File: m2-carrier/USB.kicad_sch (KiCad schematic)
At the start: 3 parts, among them P7 USB_C_Plug, U4 USBLC6-2SC6

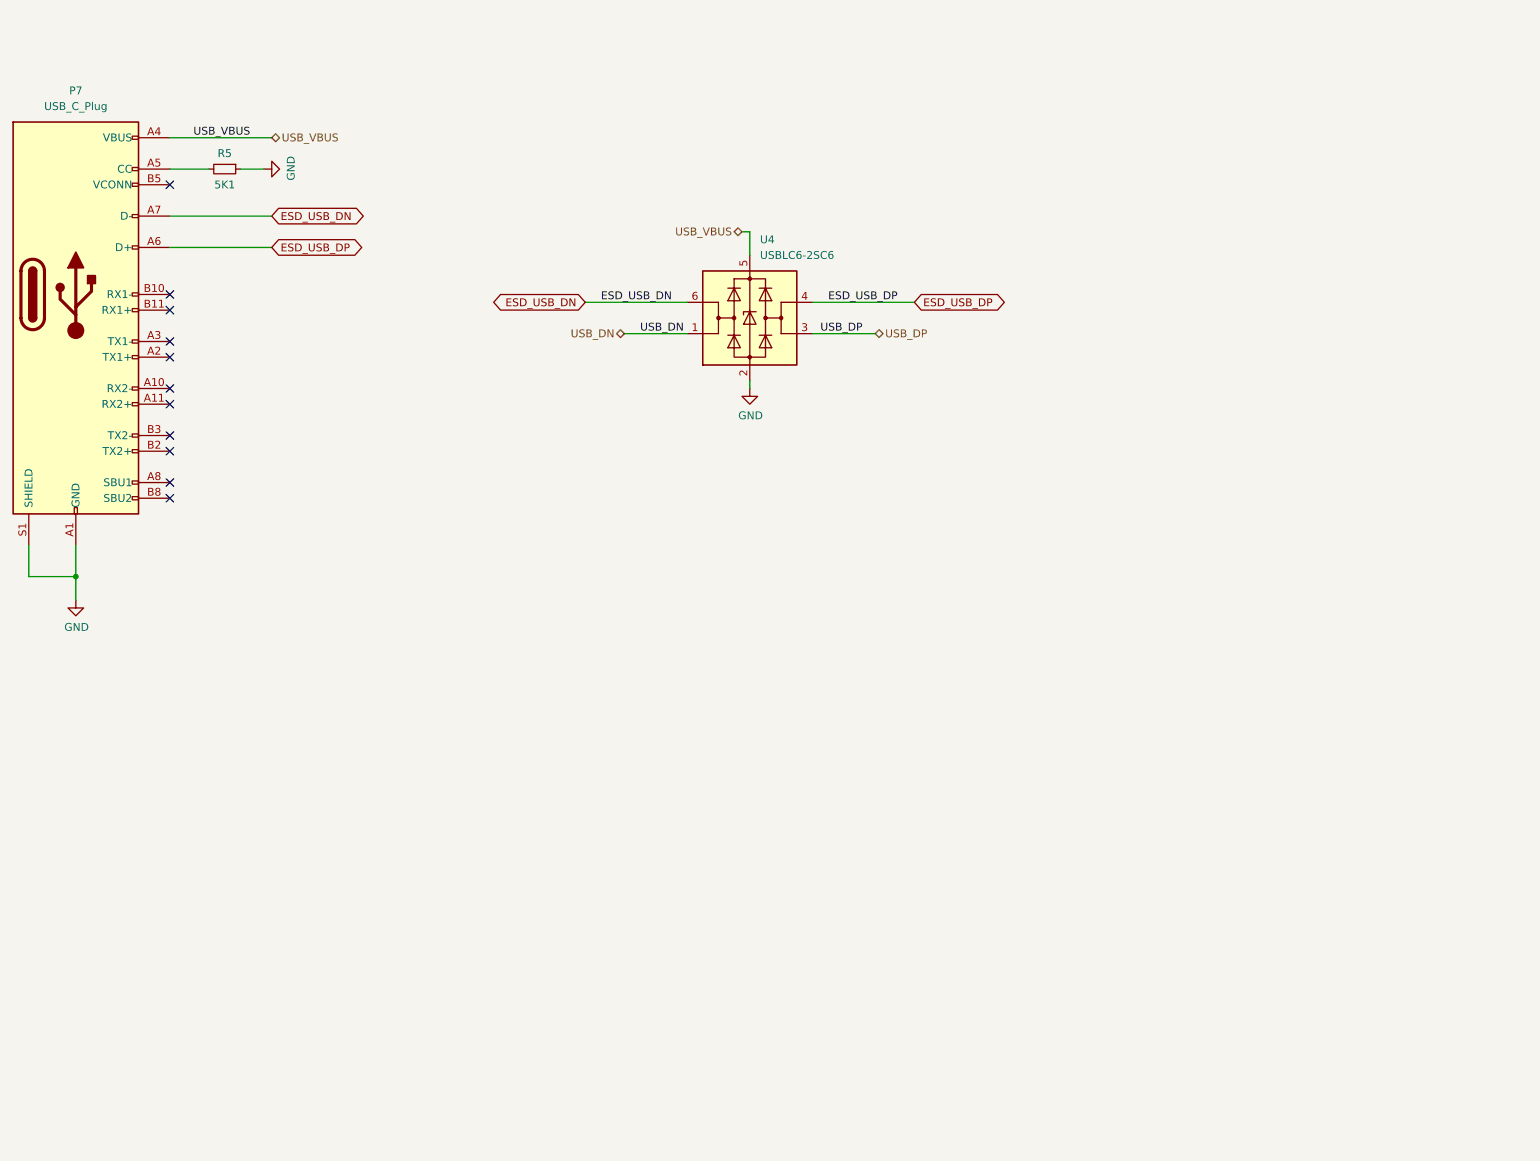
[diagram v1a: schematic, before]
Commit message: added video IC
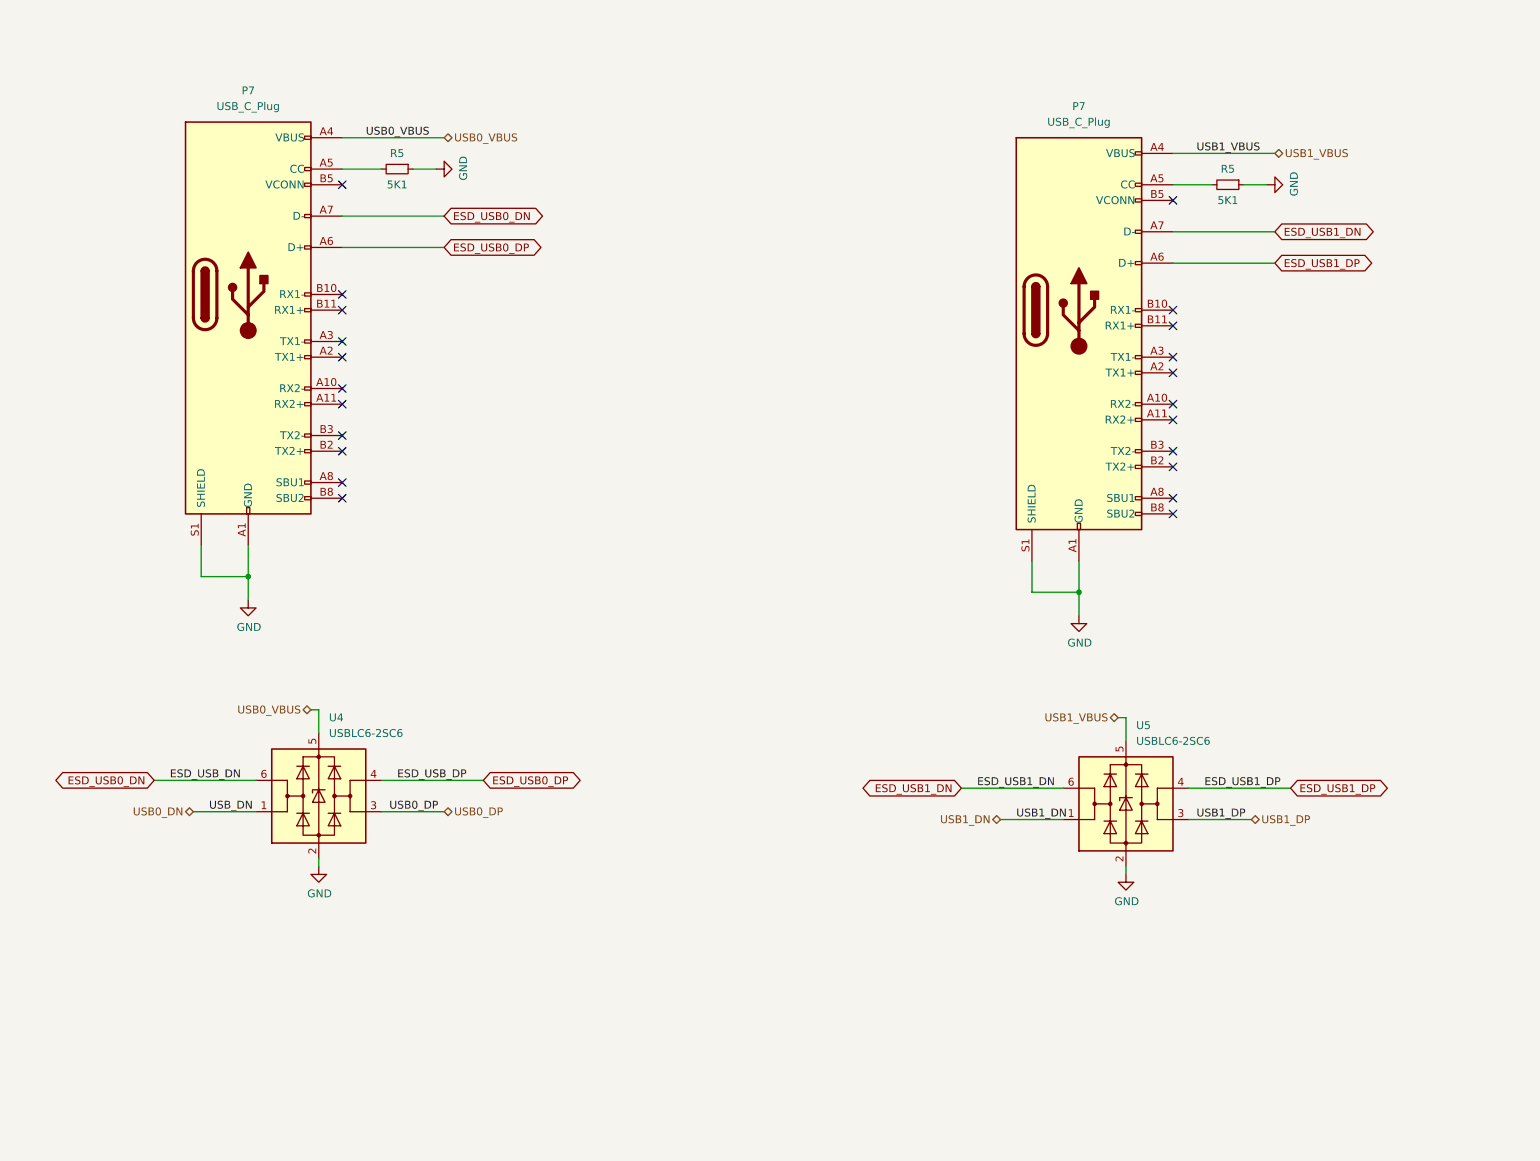
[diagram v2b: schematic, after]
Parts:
- added P7: USB_C_Plug, symbol Connector:USB_C_Plug
- added R5: 5K1, symbol Device:R_Small
- added U5: USBLC6-2SC6, Package_TO_SOT_SMD:SOT-23-6, symbol Power_Protection:USBLC6-2SC6
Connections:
- net GND: now also P7.A1 (GND), P7.A12 (GND), P7.B1 (GND), P7.B12 (GND), P7.S1 (SHIELD), R5.1, U5.2 (GND)
- net ESD_USB_DN renamed ESD_USB0_DN
- net ESD_USB_DP renamed ESD_USB0_DP
- net USB_DN renamed USB0_DN
- net USB_DP renamed USB0_DP
- net USB_VBUS renamed USB0_VBUS
- new net: P7.A5 (CC), R5.2
- new net ESD_USB1_DN: P7.A7 (D-), U5.6 (I/O1)
- new net ESD_USB1_DP: P7.A6 (D+), U5.4 (I/O2)
- new net USB1_DN: U5.1 (I/O1)
- new net USB1_DP: U5.3 (I/O2)
- new net USB1_VBUS: P7.A4 (VBUS), P7.A9 (VBUS), P7.B4 (VBUS), P7.B9 (VBUS), U5.5 (VBUS)
- no-connect marks 11 -> 22
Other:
- moved on the sheet: P7, R5, U4

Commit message: Added base board
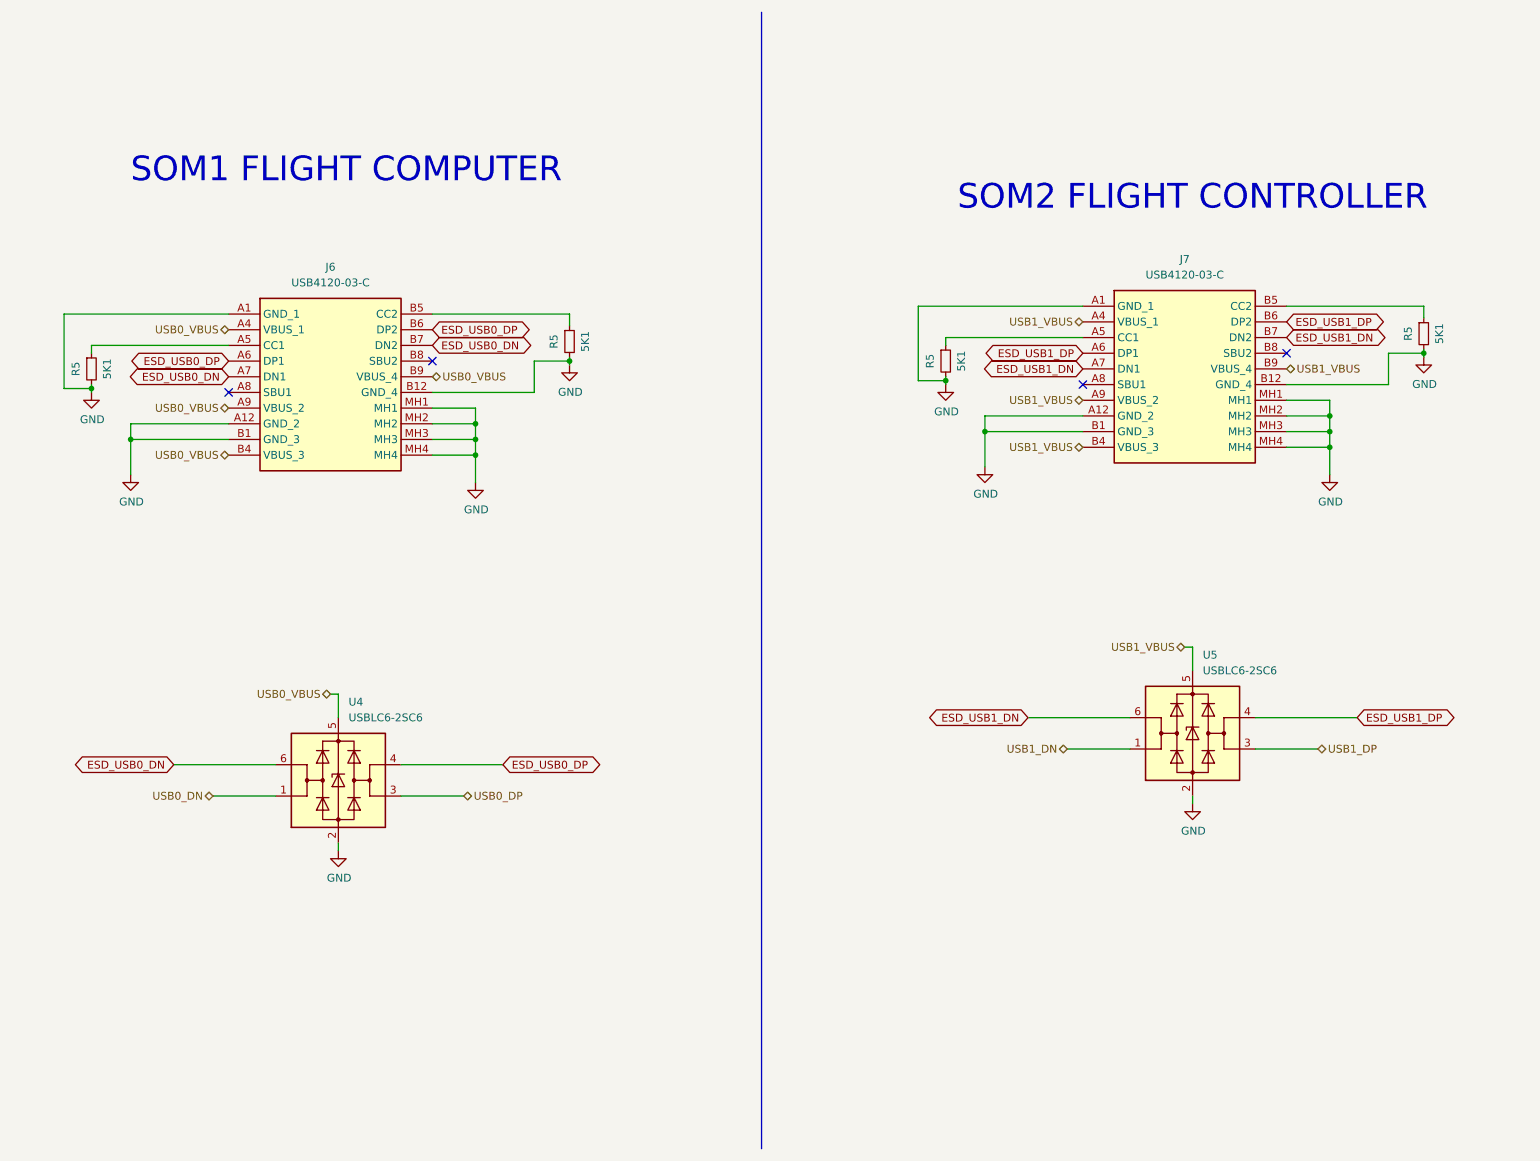
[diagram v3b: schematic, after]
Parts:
- removed P7 (x2): USB_C_Plug, symbol Connector:USB_C_Plug
- removed R5 (x2): 5K1, symbol Device:R_Small
- added J6, J7: USB4120-03-C, USB4120:USB412003C, symbol USB4120-03-C:USB4120-03-C
- added R5 (x4): 5K1, Resistor_SMD:R_0402_1005Metric, symbol Device:R_Small
- U4, U5: LCSC (none) -> C7519
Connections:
- net ESD_USB0_DN: now also J6.A7 (DN1), J6.B7 (DN2)
- net ESD_USB0_DP: now also J6.A6 (DP1), J6.B6 (DP2)
- net ESD_USB1_DN: now also J7.A7 (DN1), J7.B7 (DN2)
- net ESD_USB1_DP: now also J7.A6 (DP1), J7.B6 (DP2)
- net GND: now also J6.A1 (GND_1), J6.A12 (GND_2), J6.B1 (GND_3), J6.B12 (GND_4), J6.MH1, J6.MH2, J6.MH3, J6.MH4, J7.A1 (GND_1), J7.A12 (GND_2), J7.B1 (GND_3), J7.B12 (GND_4), J7.MH1, J7.MH2, J7.MH3, J7.MH4, R5.2, R5.2, R5.2, R5.2
- net USB0_VBUS: now also J6.A4 (VBUS_1), J6.A9 (VBUS_2), J6.B4 (VBUS_3), J6.B9 (VBUS_4)
- net USB1_VBUS: now also J7.A4 (VBUS_1), J7.A9 (VBUS_2), J7.B4 (VBUS_3), J7.B9 (VBUS_4)
- new net: J6.A5 (CC1), R5.1
- new net: J7.A5 (CC1), R5.1
- new net: J7.B5 (CC2), R5.1
- new net: J6.B5 (CC2), R5.1
- no-connect marks 22 -> 4
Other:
- note added: "SOM1 FLIGHT COMPUTER"
- note added: "SOM2 FLIGHT CONTROLLER"
- moved on the sheet: U4
